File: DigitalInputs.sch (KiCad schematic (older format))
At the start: 3 parts

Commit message: Checkpoint before trying 4 layer
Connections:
- no-connect marks 0 -> 1
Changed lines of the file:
@@
 $Descr A4 11693 8268
 encoding utf-8
-Sheet 48 50
+Sheet 33 37
 Title ""
 Date ""
@@
 AR Path="/6140E4B1/60430247" Ref="R31"  Part="1"
 AR Path="/6142CFEB/60430247" Ref="R38"  Part="1"
-F 0 "R31" V 2645 2750 50  0000 C CNN
+AR Path="/61EEF5C6/60430247" Ref="R33"  Part="1"
+F 0 "R33" V 2645 2750 50  0000 C CNN
 F 1 "4K7" V 2736 2750 50  0000 C CNN
 F 2 "Resistor_SMD:R_0805_2012Metric" V 2890 2740 50  0001 C CNN
@@
 AR Path="/6140E4B1/604306A1" Ref="R32"  Part="1"
 AR Path="/6142CFEB/604306A1" Ref="R39"  Part="1"
-F 0 "R32" H 3218 3196 50  0000 L CNN
+AR Path="/61EEF5C6/604306A1" Ref="R34"  Part="1"
+F 0 "R34" H 3218 3196 50  0000 L CNN
 F 1 "1K5" H 3218 3105 50  0000 L CNN
 F 2 "Resistor_SMD:R_0805_2012Metric" V 3190 3140 50  0001 C CNN
@@
 AR Path="/6140E4B1/60430B80" Ref="C33"  Part="1"
 AR Path="/6142CFEB/60430B80" Ref="C34"  Part="1"
-F 0 "C33" H 3715 3196 50  0000 L CNN
+AR Path="/61EEF5C6/60430B80" Ref="C4"  Part="1"
+F 0 "C4" H 3715 3196 50  0000 L CNN
 F 1 "1uF" H 3715 3105 50  0000 L CNN
 F 2 "Capacitor_SMD:C_0805_2012Metric" H 3600 3150 50  0001 C CNN
@@
 Text HLabel 3350 3500 0    50   Input ~ 0
 GND
+NoConn ~ 5100 -1450
 $EndSCHEMATC

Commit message: Routed PCB
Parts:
- C10: JLCPCB_PN (none) -> C28323
- R5: JLCPCB_PN (none) -> C17673
- R6: JLCPCB_PN (none) -> C4310
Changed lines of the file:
@@
 F 2 "Resistor_SMD:R_0805_2012Metric" V 2890 2740 50  0001 C CNN
 F 3 "~" H 2850 2750 50  0001 C CNN
+F 4 "C17673" H 2850 2750 50  0001 C CNN "JLCPCB_PN"
 	1    2850 2750
 	0    1    1    0
@@
 F 2 "Resistor_SMD:R_0805_2012Metric" V 3190 3140 50  0001 C CNN
 F 3 "~" H 3150 3150 50  0001 C CNN
+F 4 "C4310" H 3150 3150 50  0001 C CNN "JLCPCB_PN"
 	1    3150 3150
 	1    0    0    -1
@@
 F 2 "Capacitor_SMD:C_0805_2012Metric" H 3600 3150 50  0001 C CNN
 F 3 "~" H 3600 3150 50  0001 C CNN
+F 4 "C28323" H 3600 3150 50  0001 C CNN "JLCPCB_PN"
 	1    3600 3150
 	1    0    0    -1

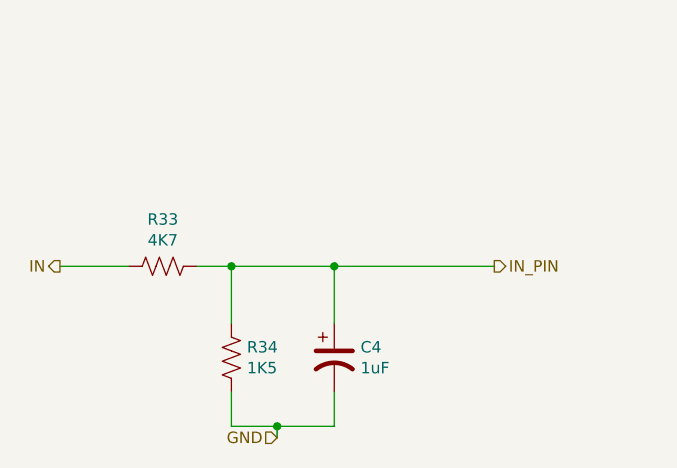
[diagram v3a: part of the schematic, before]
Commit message: Checkpoint 2022-01-19
Design with bluepill to run the heater since we lose some of the SPI
pins to the USB port on the STM32-H107.
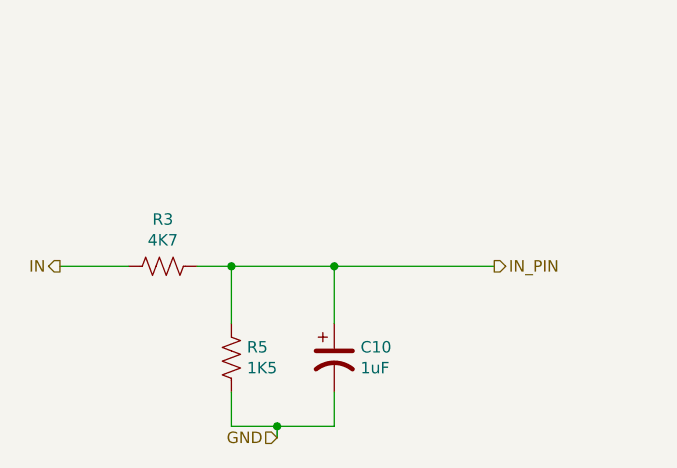
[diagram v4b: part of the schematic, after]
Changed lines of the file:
@@
 $Descr A4 11693 8268
 encoding utf-8
-Sheet 26 36
+Sheet 25 37
 Title ""
 Date ""
@@
 AR Path="/6142CFEB/60430247" Ref="R38"  Part="1"
 AR Path="/61EEF5C6/60430247" Ref="R33"  Part="1"
-F 0 "R33" V 2645 2750 50  0000 C CNN
+F 0 "R3" V 2645 2750 50  0000 C CNN
 F 1 "4K7" V 2736 2750 50  0000 C CNN
 F 2 "Resistor_SMD:R_0805_2012Metric" V 2890 2740 50  0001 C CNN
@@
 AR Path="/6142CFEB/604306A1" Ref="R39"  Part="1"
 AR Path="/61EEF5C6/604306A1" Ref="R34"  Part="1"
-F 0 "R34" H 3218 3196 50  0000 L CNN
+F 0 "R5" H 3218 3196 50  0000 L CNN
 F 1 "1K5" H 3218 3105 50  0000 L CNN
 F 2 "Resistor_SMD:R_0805_2012Metric" V 3190 3140 50  0001 C CNN
@@
 AR Path="/6142CFEB/60430B80" Ref="C34"  Part="1"
 AR Path="/61EEF5C6/60430B80" Ref="C4"  Part="1"
-F 0 "C4" H 3715 3196 50  0000 L CNN
+F 0 "C10" H 3715 3196 50  0000 L CNN
 F 1 "1uF" H 3715 3105 50  0000 L CNN
 F 2 "Capacitor_SMD:C_0805_2012Metric" H 3600 3150 50  0001 C CNN
